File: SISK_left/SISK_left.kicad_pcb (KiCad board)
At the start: 2 copper layers, 142.1 x 121.8 mm, 71 parts, among them J1 OLED_128x32, J2 BAT, J3 CONN_ALT, SW1 SW_push, SW10 SW_push, SW11 SW_push, SW12 SW_push, SW13 SW_push, SW14 SW_push, SW15 SW_push, SW16 SW_push, SW17 SW_push, SW18 SW_push, SW19 SW_push, SW2 SW_push, SW20 SW_push, SW21 SW_push, SW22 SW_push, SW23 SW_push, SW24 SW_push, SW25 SW_push, SW26 SW_push, SW27 SW_push, SW28 SW_push, SW29 SW_push, SW3 SW_push, SW30 SW_push, SW31 SW_SPDT, SW4 SW_push, SW5 SW_push, SW6 SW_push, SW7 SW_push, SW8 SW_push, SW9 SW_push, U1 Nice_Nano_V2

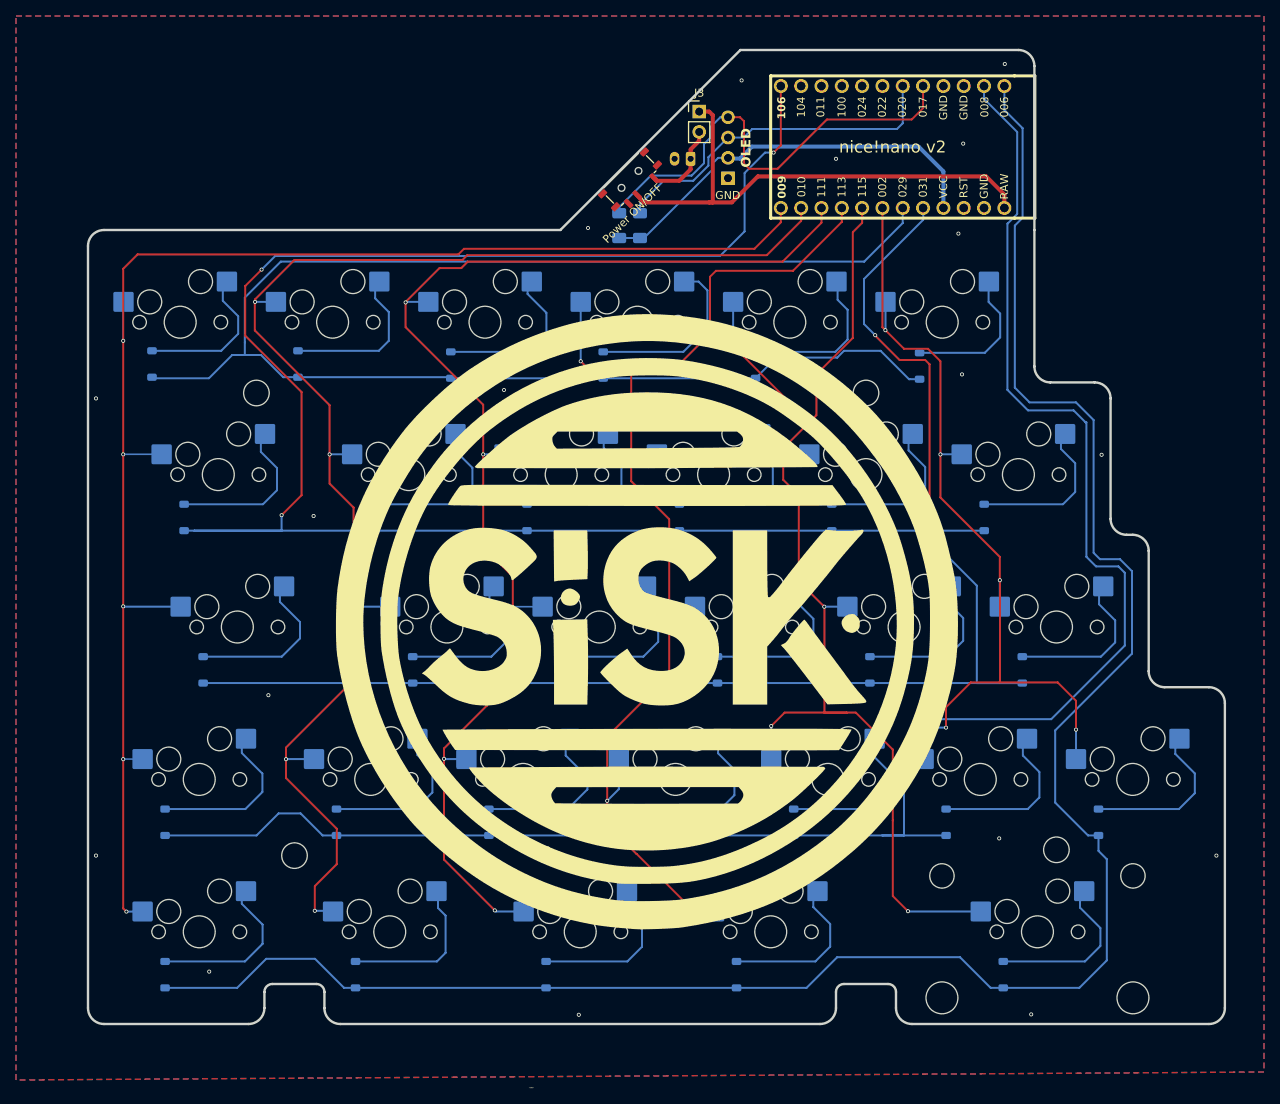
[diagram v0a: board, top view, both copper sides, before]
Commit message: improved the whole mounting hole situation
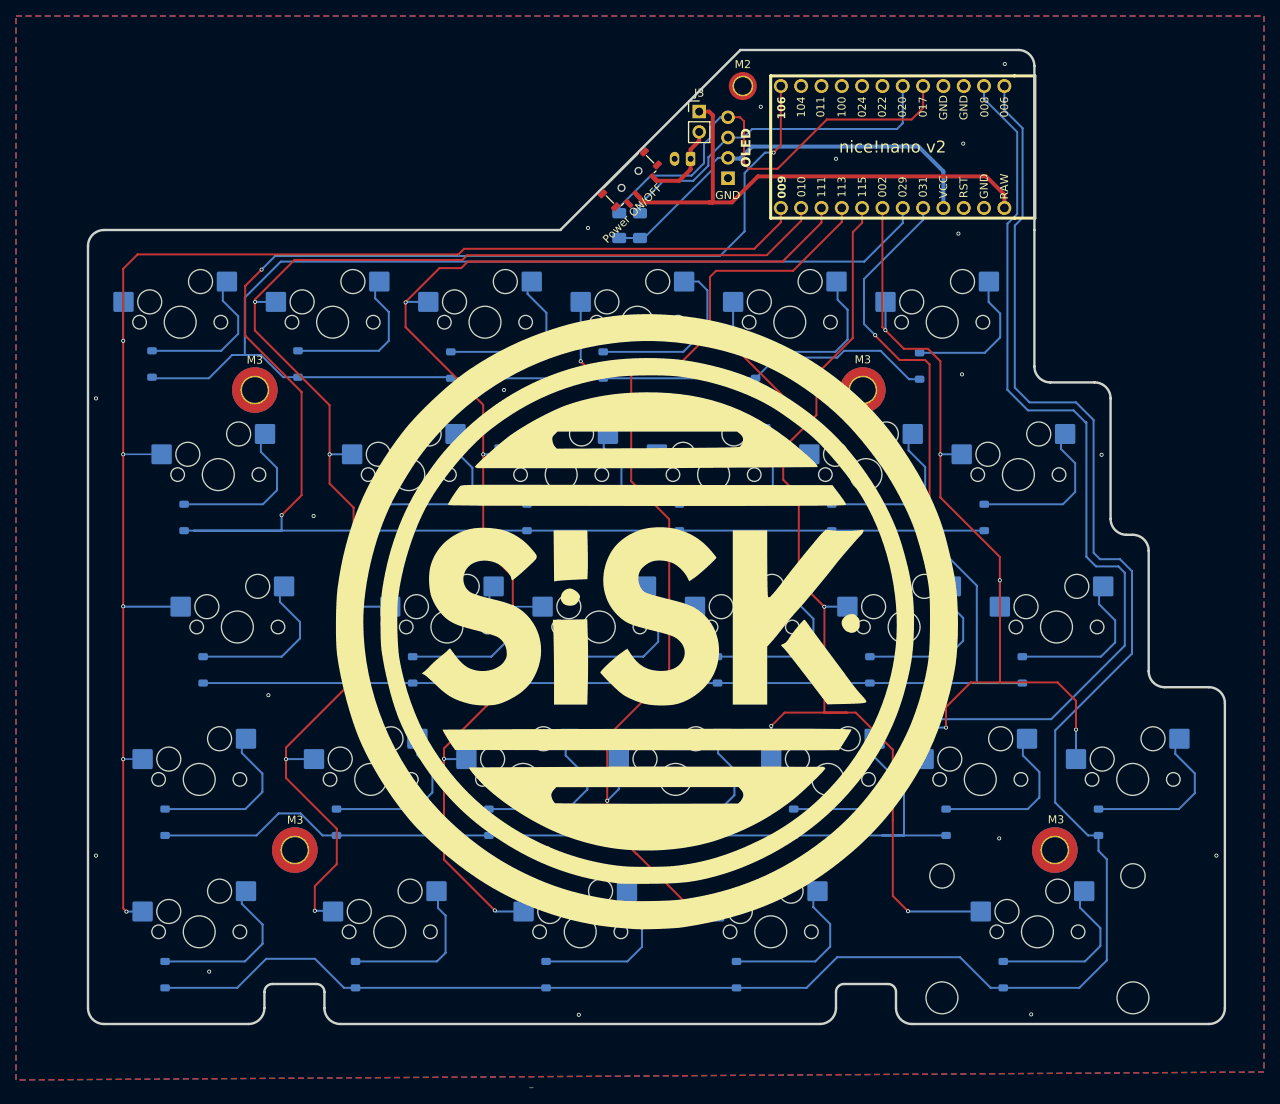
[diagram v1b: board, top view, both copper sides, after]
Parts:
- removed REF** (x4): MountingHole_3.2mm_M3_ISO7380, MountingHole:MountingHole_3.2mm_M3_ISO7380
- added H1: M3, MountingHole:MountingHole_3.2mm_M3_ISO7380_Pad_TopBottom, F.Cu at (284.0, 310.5)
- added H2: M3, MountingHole:MountingHole_3.2mm_M3_ISO7380_Pad_TopBottom, F.Cu at (189.0, 310.5)
- added H3: M3, MountingHole:MountingHole_3.2mm_M3_ISO7380_Pad_TopBottom, F.Cu at (184.0, 253.0)
- added H4: M3, MountingHole:MountingHole_3.2mm_M3_ISO7380_Pad_TopBottom, F.Cu at (260.0, 253.0)
- added H5: M2, MountingHole:MountingHole_2.2mm_M2_ISO7380_Pad_TopOnly, F.Cu at (245.0, 215.0)

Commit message: last changes on silkscreen before manufaturing
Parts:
- moved SW31 0.42 mm to (230.6, 226.4)
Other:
- outline, holes or cut-outs redrawn
- board text added: "ON/OFF SW"
- board text removed: "Power ON/OFF"
